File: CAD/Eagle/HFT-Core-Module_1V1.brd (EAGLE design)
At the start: 96.5 x 96.5 mm, 526 parts, among them Q0321 ABS07-32.768KHZ, Q1321 ABS07-32.768KHZ, Q2211 ABM3B-32.0000MHZ, Q2311 ABM3B-16.0000MHZ, T1051 MMBT2222, T1111 MMBT2222, T1121 MMBT2222, T1131 MMBT2222, U0111 STM32L4Z_144PIN_SMPS, U0521 PCAL6416APW, U0621 PCAL6416APW, U0711 IS25LP032D, U0721 IS25LP032D, U0801 CAT24C64, U0911 ZIO_EINK_1IN54, U1001 MIDAS_MCCOG21605B6W-FPTLWI, U1301 BNO085, U1401 BME680, U1501 LM4120IM5-3.0, U1511 MAX5217, U1531 CFPT-141-20MHZ, U1541 OPA354, U1542 LPV811, U1601 Si5338, U1651 TS5A23166, U1701 PCM1863, U1801 WM8523, U1901 SIM868, U2001 74LVC4245A, U2101 74LVC4245A, U2201 SX1262, U2271 PE4259, U2301 AX5243, U2401 LM53603-Q1, U2501 BQ24193, U2541 LPV811, U2601 BQ25570, U2681 TS5A23166, U2701 TPS62051, U2751 MCP4661-104E-MS, U2801 TS5A23166, U2901 TS5A23166, U3001 TS5A23166, U3101 TS5A23166, U3391 TS5A23166, U3392 TDK B4310, X1201 TTE_EN11-HSM, X1951 MICROSIM-8P_SDCARD-8P_MOLEX-1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, X2411 WIRE-TO-BOARD_5MM08_1X02, X2551 JST_S3B-XH-A, X2601 WIRE-TO-BOARD_5MM08_1X02, X3201 MOLEX 105017-0001, X3301 SMA_SMT_AMPHENOL-901-143, X3311 SAMTEC SMA-J-P-H-RA-TH1, X3371 SMA_SMT_AMPHENOL-901-143, SAM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, X3381 SMA_SMT_AMPHENOL-901-143, SAM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, X3391 SMA_SMT_AMPHENOL-901-143, SAM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, X3401 CUI SJ1-3535NS, X3411 CUI SJ1-3535NS, X3511 2X20/90_1MM27_HARWIN_M50-3202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, X3512 2X20/90_1MM27_HARWIN_M50-3202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, X3531 2X20/90_1MM27_HARWIN_M50-3202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, X3532 2X20/90_1MM27_HARWIN_M50-3202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

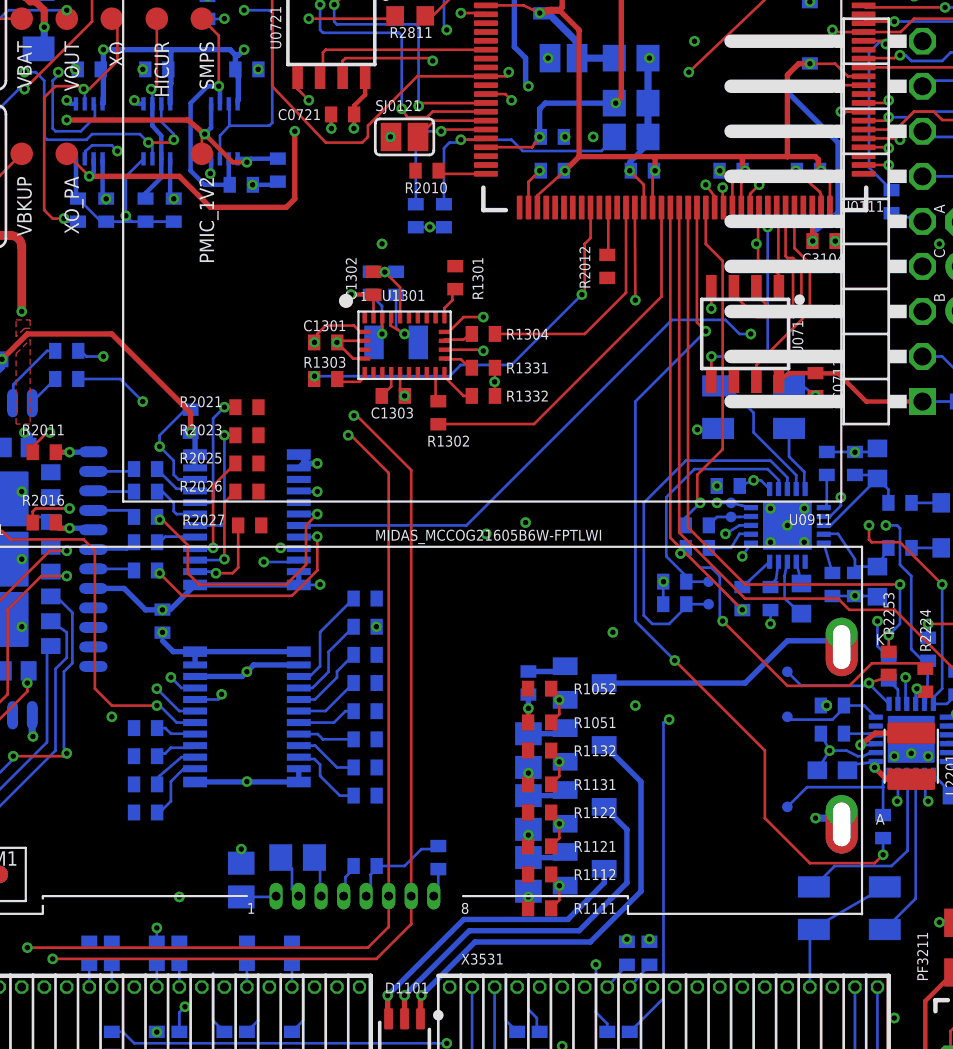
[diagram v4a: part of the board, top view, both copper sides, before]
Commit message: HW_1V1 - CAD/Eagle - some more wires routed in the south
Signed-off-by: Ulrich Habel <espero7757@gmx.net>
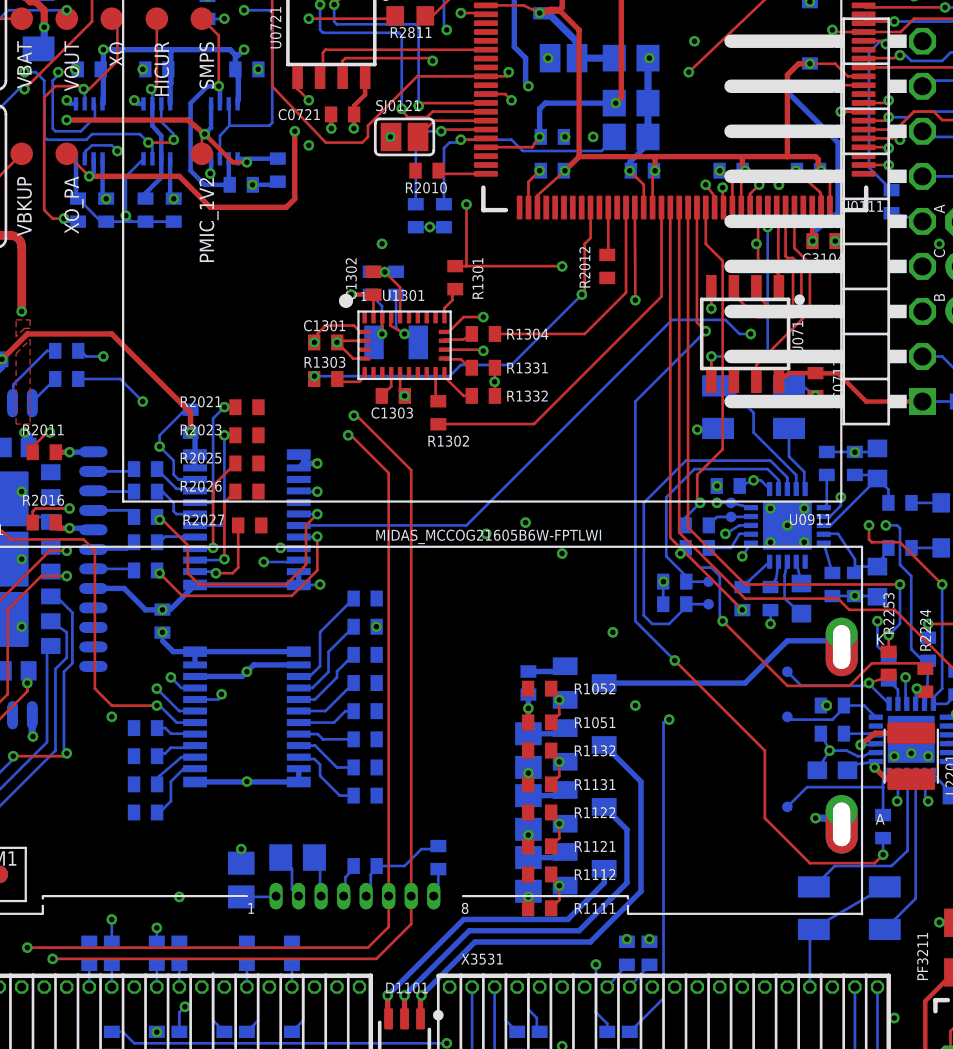
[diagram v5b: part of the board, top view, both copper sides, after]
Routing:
- net PD11: track 64.0 -> 148.6 mm, vias 6 -> 9
- net PC11: track 57.1 -> 103.2 mm, vias 4 -> 8
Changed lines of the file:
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@@
 <grid distance="50" unitdist="mil" unit="mil" style="lines" multiple="1" display="yes" altdistance="6.25" altunitdist="mil" altunit="mil"/>
 <layers>
-<layer number="1" name="Top" color="4" fill="1" visible="no" active="yes"/>
+<layer number="1" name="Top" color="4" fill="1" visible="yes" active="yes"/>
 <layer number="2" name="Route2" color="1" fill="3" visible="yes" active="yes"/>
 <layer number="3" name="Route3" color="4" fill="3" visible="no" active="no"/>
@@
 <wire x1="73.025" y1="63.65875" x2="73.025" y2="55.88" width="0.1524" layer="15"/>
 <wire x1="73.025" y1="55.88" x2="72.86625" y2="55.72125" width="0.1524" layer="15"/>
-<wire x1="31.75" y1="8.905" x2="72.8775" y2="55.71" width="0" layer="19" extent="1-16"/>
+<via x="72.8775" y="55.71" extent="1-2" drill="0.3048"/>
+<wire x1="72.8775" y1="55.71" x2="60.94875" y2="55.71" width="0.1524" layer="2"/>
+<wire x1="60.94875" y1="55.71" x2="60.80125" y2="55.5625" width="0.1524" layer="2"/>
+<wire x1="60.80125" y1="55.5625" x2="49.8475" y2="55.5625" width="0.1524" layer="2"/>
+<wire x1="49.8475" y1="55.5625" x2="49.53" y2="55.245" width="0.1524" layer="2"/>
+<wire x1="49.53" y1="55.245" x2="46.6725" y2="55.245" width="0.1524" layer="2"/>
+<wire x1="46.6725" y1="55.245" x2="46.51375" y2="55.40375" width="0.1524" layer="2"/>
+<wire x1="46.51375" y1="55.40375" x2="43.18" y2="55.40375" width="0.1524" layer="2"/>
+<wire x1="43.18" y1="55.40375" x2="43.02125" y2="55.245" width="0.1524" layer="2"/>
+<wire x1="43.02125" y1="55.245" x2="43.02125" y2="53.975" width="0.1524" layer="2"/>
+<wire x1="43.02125" y1="53.975" x2="42.8625" y2="53.81625" width="0.1524" layer="2"/>
+<via x="42.8625" y="53.81625" extent="1-16" drill="0.3048"/>
+<wire x1="42.8625" y1="53.81625" x2="43.02125" y2="53.6575" width="0.1524" layer="15"/>
+<wire x1="43.02125" y1="53.6575" x2="43.02125" y2="46.99" width="0.1524" layer="15"/>
+<wire x1="43.02125" y1="46.99" x2="40.64" y2="44.60875" width="0.1524" layer="15"/>
+<wire x1="40.64" y1="44.60875" x2="40.64" y2="31.90875" width="0.1524" layer="15"/>
+<wire x1="40.64" y1="31.90875" x2="39.6875" y2="30.95625" width="0.1524" layer="15"/>
+<wire x1="39.6875" y1="30.95625" x2="39.6875" y2="24.92375" width="0.1524" layer="15"/>
+<wire x1="39.6875" y1="24.92375" x2="40.16375" y2="24.4475" width="0.1524" layer="15"/>
+<wire x1="40.16375" y1="24.4475" x2="40.16375" y2="22.86" width="0.1524" layer="15"/>
+<wire x1="40.16375" y1="22.86" x2="37.1475" y2="19.84375" width="0.1524" layer="15"/>
+<wire x1="37.1475" y1="19.84375" x2="37.1475" y2="10.63625" width="0.1524" layer="15"/>
+<wire x1="37.1475" y1="10.63625" x2="36.83" y2="10.31875" width="0.1524" layer="15"/>
+<wire x1="36.83" y1="10.31875" x2="31.90875" y2="10.31875" width="0.1524" layer="15"/>
+<wire x1="31.90875" y1="10.31875" x2="31.75" y2="10.16" width="0.1524" layer="15"/>
+<via x="31.75" y="10.16" extent="15-16" drill="0.3048"/>
+<wire x1="31.75" y1="10.16" x2="31.75" y2="8.905" width="0.1524" layer="16"/>
 </signal>
 <signal name="PD10">
@@
 <wire x1="64.12" y1="30.8125" x2="63.8325" y2="30.8125" width="0.1524" layer="16"/>
 <wire x1="63.8325" y1="30.8125" x2="63.8175" y2="30.7975" width="0.1524" layer="16"/>
-<wire x1="63.8175" y1="30.7975" x2="58.42" y2="30.7975" width="0.1524" layer="2"/>
+<wire x1="63.8175" y1="30.7975" x2="57.15" y2="30.7975" width="0.1524" layer="2"/>
 <wire x1="70.75" y1="71.61" x2="70.64375" y2="71.50375" width="0.1524" layer="1"/>
 <wire x1="70.64375" y1="71.50375" x2="70.64375" y2="70.64375" width="0.1524" layer="1"/>
@@
 <wire x1="70.8025" y1="65.24625" x2="70.1675" y2="64.61125" width="0.1524" layer="15"/>
 <wire x1="70.1675" y1="64.61125" x2="70.1675" y2="59.3725" width="0.1524" layer="15"/>
-<wire x1="70.1675" y1="59.3725" x2="69.5325" y2="58.7375" width="0.1524" layer="15"/>
-<wire x1="69.5325" y1="58.7375" x2="69.5325" y2="52.07" width="0.1524" layer="15"/>
-<wire x1="51.1175" y1="47.005" x2="69.5325" y2="52.07" width="0" layer="19" extent="1-15"/>
-<wire x1="58.42" y1="30.7975" x2="51.1175" y2="47.005" width="0" layer="19" extent="1-2"/>
+<wire x1="70.1675" y1="59.3725" x2="69.69125" y2="58.89625" width="0.1524" layer="15"/>
+<wire x1="69.69125" y1="58.89625" x2="69.69125" y2="53.49875" width="0.1524" layer="15"/>
+<wire x1="69.69125" y1="53.49875" x2="69.37375" y2="53.18125" width="0.1524" layer="15"/>
+<wire x1="69.37375" y1="53.18125" x2="69.37375" y2="51.59375" width="0.1524" layer="15"/>
+<via x="69.37375" y="51.59375" extent="1-16" drill="0.3048"/>
+<wire x1="69.37375" y1="51.59375" x2="69.37375" y2="50.64125" width="0.1524" layer="2"/>
+<wire x1="69.37375" y1="50.64125" x2="69.215" y2="50.4825" width="0.1524" layer="2"/>
+<wire x1="69.215" y1="50.4825" x2="51.7525" y2="50.4825" width="0.1524" layer="2"/>
+<via x="51.7525" y="50.4825" extent="1-2" drill="0.3048"/>
+<wire x1="51.7525" y1="50.4825" x2="51.7525" y2="47.005" width="0.1524" layer="1"/>
+<wire x1="51.1175" y1="47.005" x2="51.7525" y2="47.005" width="0.1524" layer="1"/>
+<wire x1="51.7525" y1="47.005" x2="57.135" y2="47.005" width="0.1524" layer="1"/>
+<wire x1="57.135" y1="47.005" x2="57.15" y2="46.99" width="0.1524" layer="1"/>
+<via x="57.15" y="46.99" extent="1-16" drill="0.3048"/>
+<wire x1="57.15" y1="46.99" x2="57.15" y2="30.7975" width="0.1524" layer="15"/>
+<via x="57.15" y="30.7975" extent="1-16" drill="0.3048"/>
 </signal>
 <signal name="PC10">
@@
 <via x="55.08625" y="32.54375" extent="1-16" drill="0.3048"/>
 <wire x1="55.08625" y1="32.54375" x2="54.9275" y2="32.54375" width="0.1524" layer="15"/>
-<wire x1="54.9275" y1="32.54375" x2="54.9275" y2="43.815" width="0.1524" layer="15"/>
-<wire x1="54.9275" y1="43.815" x2="54.61" y2="44.1325" width="0.1524" layer="15"/>
-<wire x1="54.61" y1="44.1325" x2="52.705" y2="44.1325" width="0.1524" layer="15"/>
+<wire x1="54.9275" y1="32.54375" x2="54.9275" y2="43.97375" width="0.1524" layer="15"/>
+<wire x1="54.9275" y1="43.97375" x2="54.76875" y2="44.1325" width="0.1524" layer="15"/>
+<wire x1="54.76875" y1="44.1325" x2="52.705" y2="44.1325" width="0.1524" layer="15"/>
 </signal>
 <signal name="MCU_SPI3_MOSI">

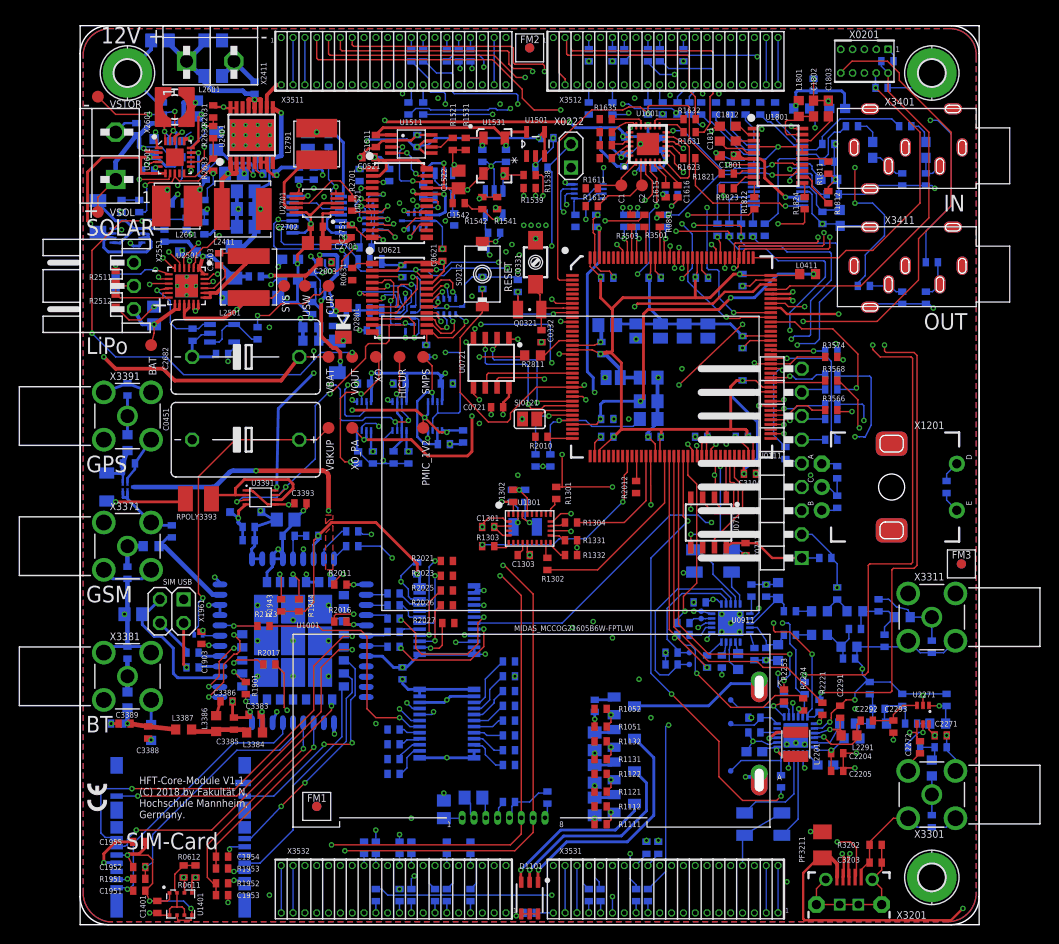
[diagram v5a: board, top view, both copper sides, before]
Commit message: HW_1V1 - CAD/Eagle - multiple DRC warnings handled, more routing done
Signed-off-by: Ulrich Habel <espero7757@gmx.net>
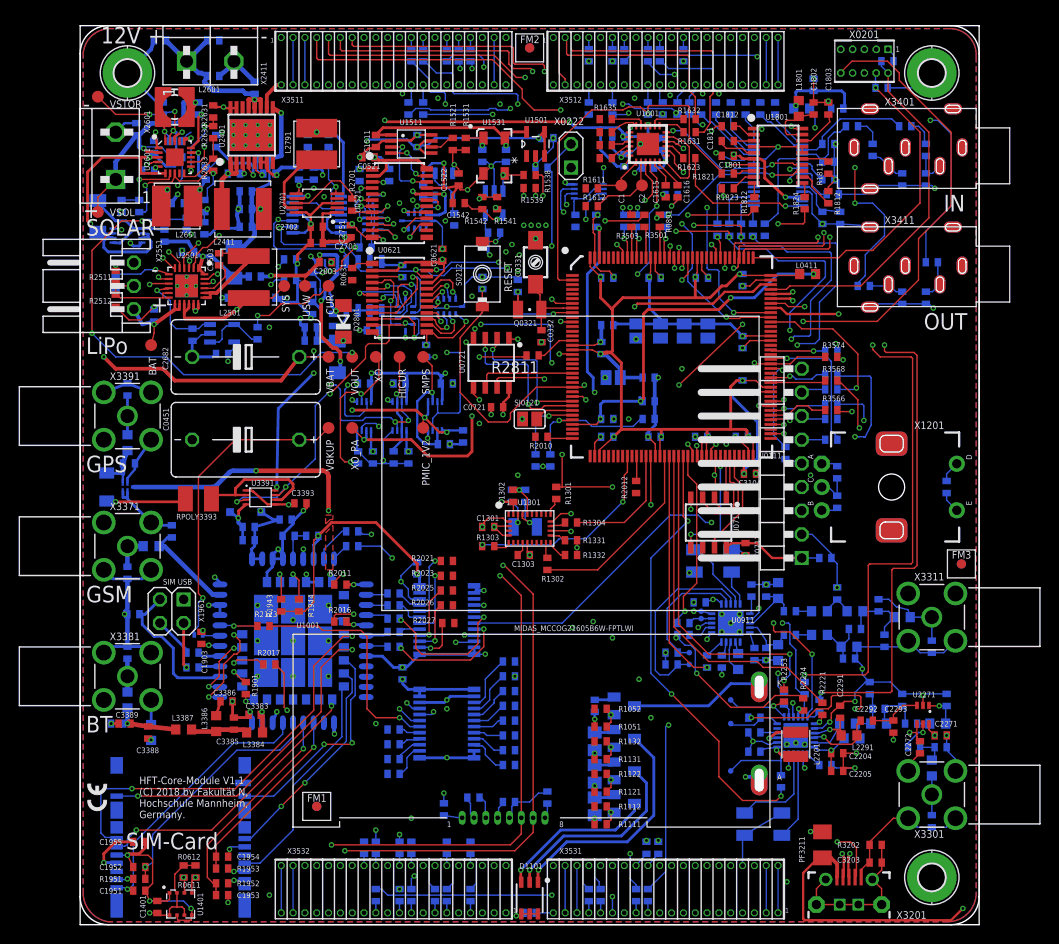
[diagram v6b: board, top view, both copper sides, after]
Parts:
- C0410, C0413, C0423, C0442, C1011, C1012, C1522, C2701, C2703: device rcl:C0805 -> df4iah_rcl:C0402
- C1701, C1704, C1706, C1801, C1802, C1803, C1811, C1812, C2201, C2203, C2501, C2502, C2521: device rcl:C0603 -> df4iah_rcl:C0402
- C1711, C1721, C2601, C2606, C2652: device df4iah_rcl:C0603 -> df4iah_rcl:C0402
- C1904, C1961, C2401, C2402, C2403, C2405, C2411, C2421, C2422, C2423, C2504, C2505, C2511: device df4iah_rcl:C0805 -> df4iah_rcl:C0402
- R2801, R2802, R2811: device df4iah_rcl:R0603 -> df4iah_rcl:R0402
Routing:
- net PEXPA_P1_6_R: track 22.9 -> 100.0 mm, vias 2 -> 3
- net GND: track 638.7 -> 643.5 mm
- net PF12: track 62.1 -> 65.8 mm, vias 6 -> 5
- net LIPO_SYS: track 50.2 -> 51.5 mm
- net PF14: track 26.2 -> 25.2 mm
- net POW_IN_5V0: track 19.9 -> 20.7 mm
- net SIM_USB_VBUS: track 16.0 -> 16.6 mm
- net DC_12V_IN: track 19.8 -> 20.3 mm
- net +3V3: track 128.7 -> 129.2 mm
- net PD11: vias 9 -> 8

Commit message: HW_1V1 - CAD/Eagle - another day routed
Signed-off-by: Ulrich Habel <espero7757@gmx.net>
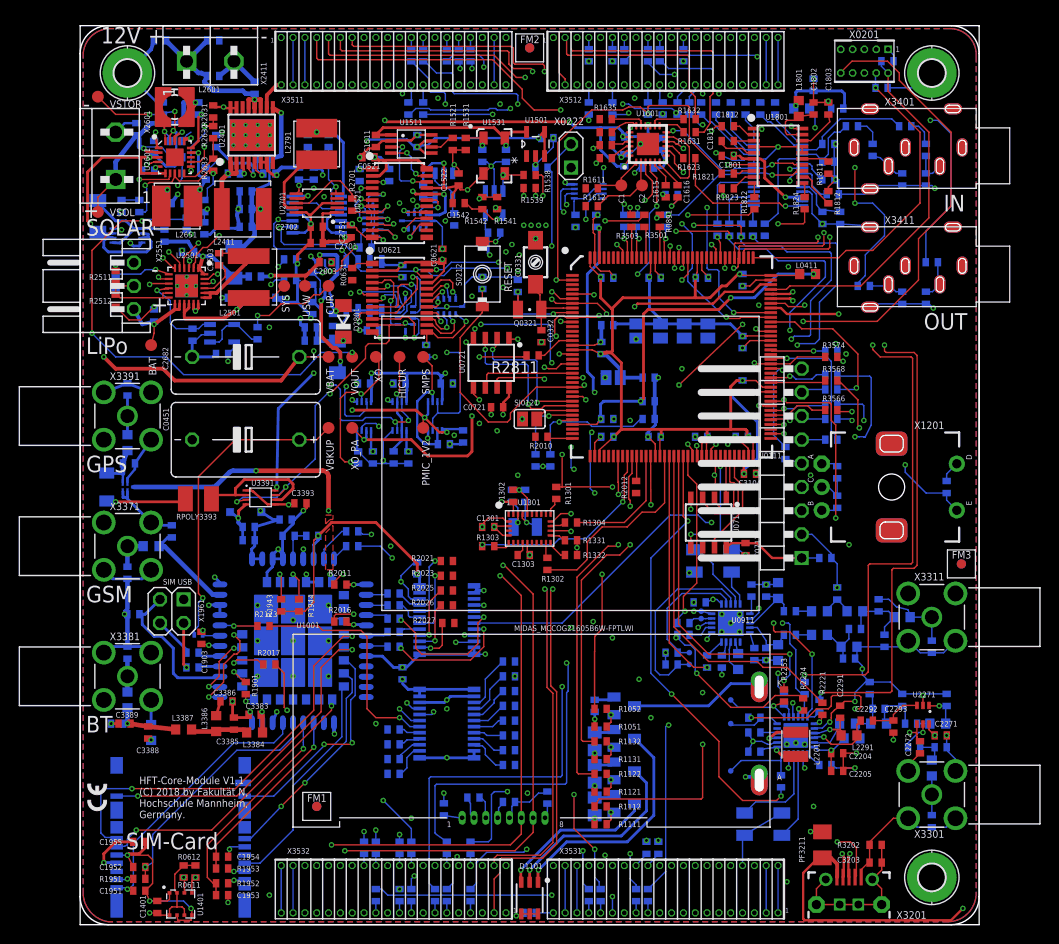
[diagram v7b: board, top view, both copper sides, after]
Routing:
- net PD3: track 29.6 -> 144.9 mm, vias 2 -> 5
- net PD12: track 52.8 -> 153.9 mm, vias 4 -> 7
- net PD1: track 58.3 -> 154.0 mm, vias 2 -> 4
- net CLK0_P: track 0.00 -> 94.3 mm, vias 0 -> 2
- net CLK0_N: track 0.00 -> 91.1 mm, vias 0 -> 2
- net PF0: track 0.00 -> 89.8 mm, vias 0 -> 4
- net PE3: track 42.4 -> 130.3 mm, vias 1 -> 4
- net PEXPB_P1_7_R: track 7.46 -> 82.6 mm, vias 1 -> 2
- net PC13: track 40.3 -> 108.9 mm, vias 3 -> 7
- net PC6: track 0.00 -> 67.7 mm, vias 0 -> 2
- net PEXPB_P1_6_R: track 5.86 -> 72.5 mm, vias 1 -> 2
- net PF8: track 3.42 -> 68.1 mm, vias 0 -> 4
- net PB15: track 62.0 -> 126.6 mm, vias 3 -> 5
- net PEXPB_P1_3_R: track 2.98 -> 64.2 mm, vias 1 -> 3
- net PF1: track 38.6 -> 98.4 mm, vias 2 -> 3
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
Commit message: HW_1V1 - CAD/Eagle - more routed, still abt. 10 airwires to do
Signed-off-by: Ulrich Habel <espero7757@gmx.net>
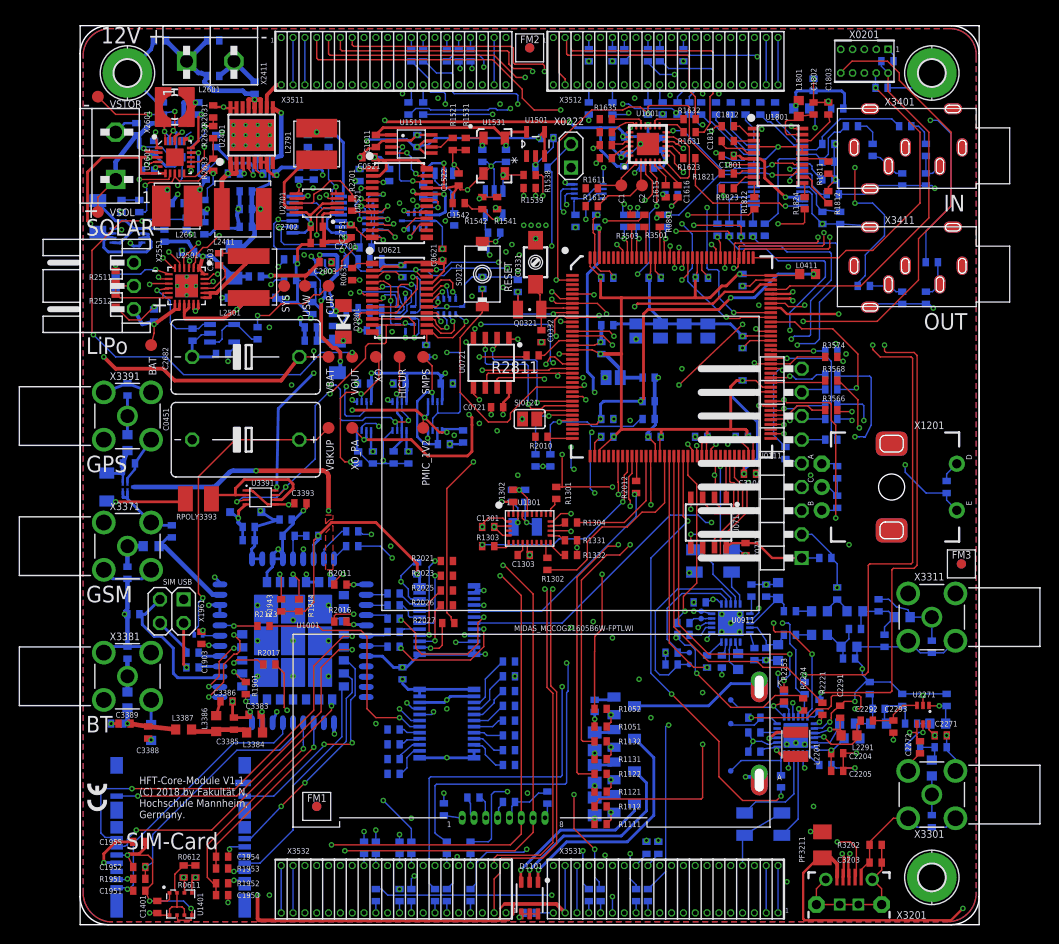
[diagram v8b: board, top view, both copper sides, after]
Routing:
- net +5V0: track 80.9 -> 216.9 mm, vias 1 -> 2
- net PF3: track 0.00 -> 78.4 mm, vias 0 -> 3
- net PF10: track 10.7 -> 57.3 mm, vias 0 -> 3
- net PF4: track 0.00 -> 41.9 mm, vias 0 -> 4
- net PF9: track 0.00 -> 39.2 mm, vias 0 -> 2
- net MCU_LPUART_RTS_OUT_R: track 0.00 -> 24.3 mm, vias 0 -> 1
- net PEXPB_P0_0_R: track 7.78 -> 29.3 mm, vias 1 -> 3
- net PEXPB_P0_1_R: track 8.24 -> 22.9 mm, vias 1 -> 2
- net PEXPB_P0_3_R: track 29.5 -> 32.4 mm
- net MCU_VDD: track 94.2 -> 95.0 mm
- net PEXPA_P0_3_R: track 43.9 -> 44.5 mm
- net PF8: track 68.1 -> 68.6 mm
